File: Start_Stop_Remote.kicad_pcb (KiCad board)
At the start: 2 copper layers, 40 x 80 mm, 65 parts, among them J1 AVR-ISP-6, Q1 AO3400A, SW1 SW_DIP_x05, SW2 Push_SW, SW3 Push_SW, SW4 Push_SW, SW6 SW_Push_DPDT, U1 ATmega168PA-AU

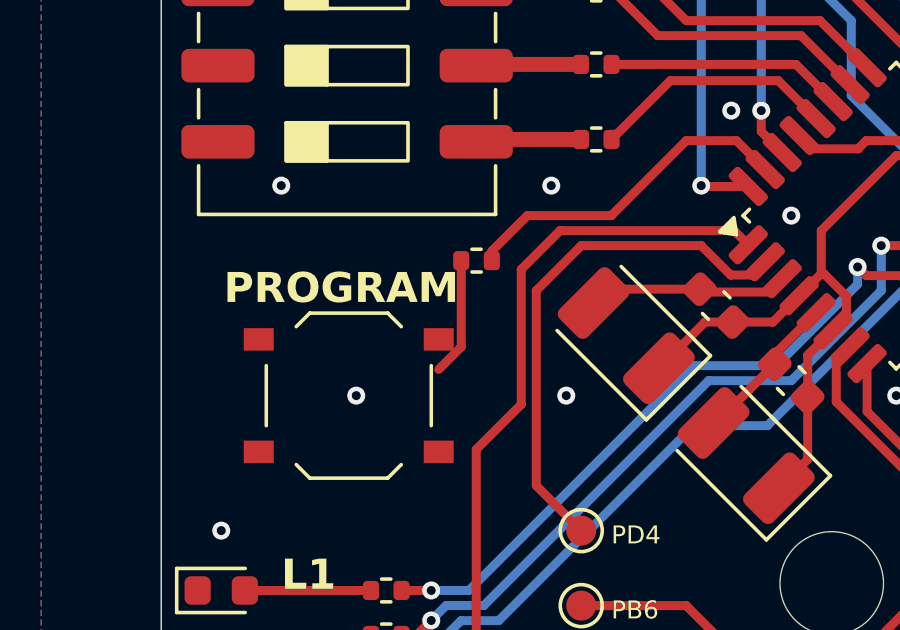
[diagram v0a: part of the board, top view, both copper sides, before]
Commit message: DRC fixes
One trace routing fix near program button.
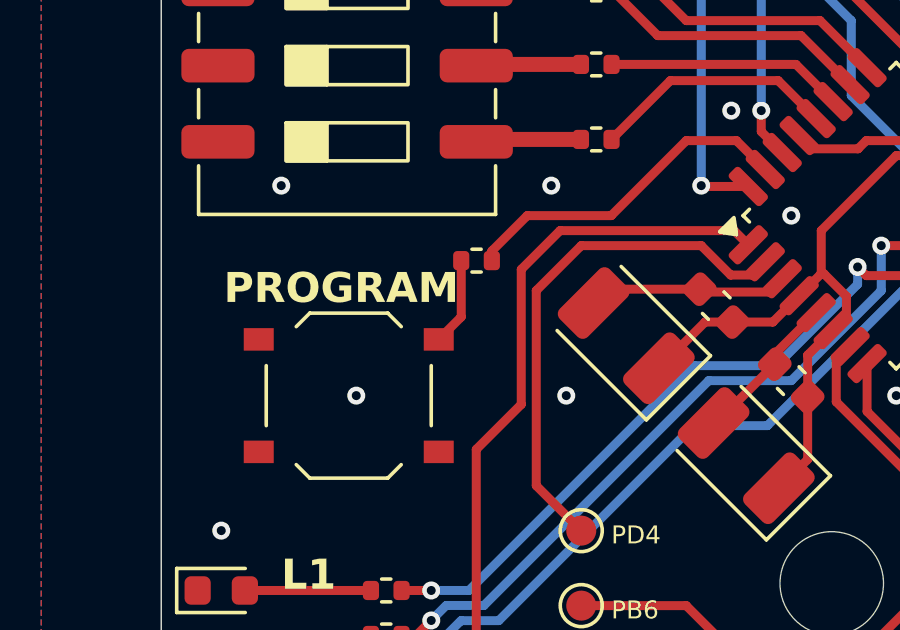
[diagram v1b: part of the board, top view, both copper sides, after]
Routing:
- net Net-(R19-Pad1): track 3.94 -> 2.94 mm
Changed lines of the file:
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@@
 	)
 	(segment
-		(start 172 103.5)
-		(end 172 106.375)
+		(start 172 105.375)
+		(end 171.25 106.125)
 		(width 0.3)
 		(layer "F.Cu")
@@
 	)
 	(segment
-		(start 172 106.375)
-		(end 171.25 107.125)
+		(start 172 103.5)
+		(end 172 105.375)
 		(width 0.3)
 		(layer "F.Cu")

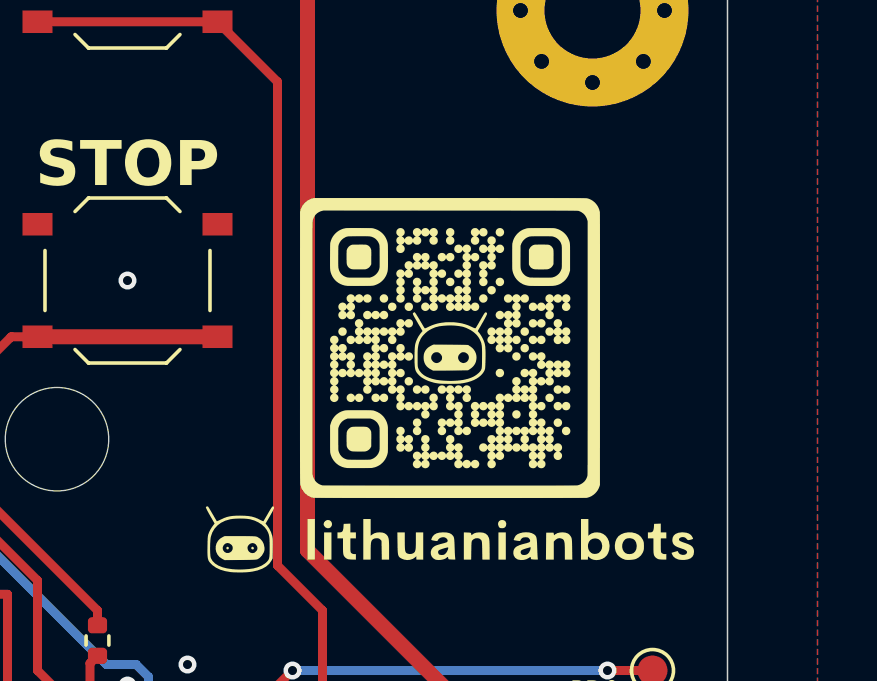
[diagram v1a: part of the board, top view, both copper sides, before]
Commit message: QR Code Update
Old QR code was linked to an external website, that has paid service. New one - just links to https://lithuanianbots.com

Library footprint updated as well.
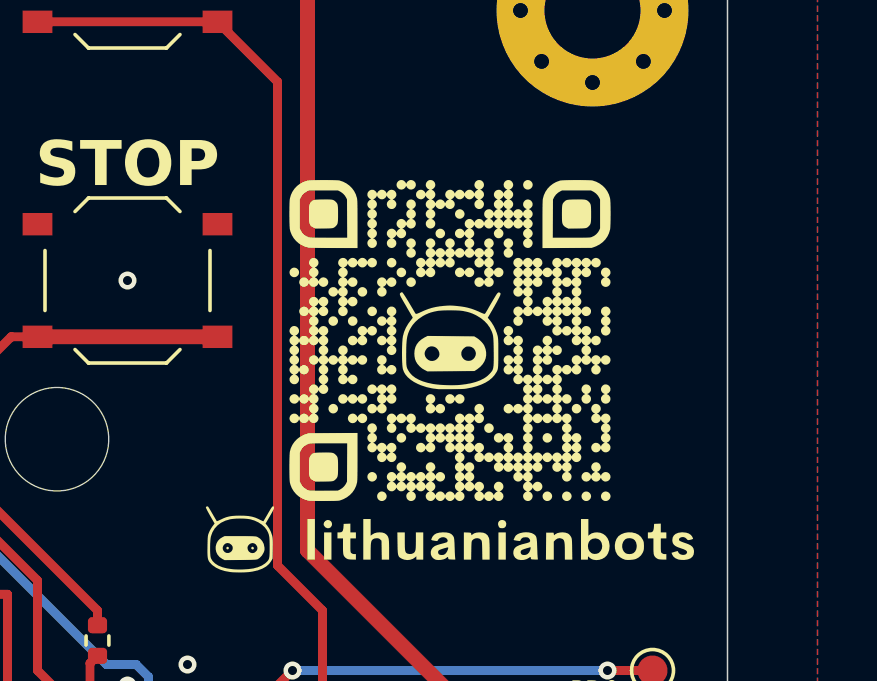
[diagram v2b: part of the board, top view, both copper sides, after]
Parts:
- removed the G*** at (192.8, 80.0)
- added G***: LOGO, _local_lib:LT_Bots_QR_12x12mm, F.Cu at (192.8, 81.0)
